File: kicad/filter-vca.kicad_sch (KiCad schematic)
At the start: 55 parts, among them J37 Conn_01x03_Male, U10 TL074, U12 LM13700, U13 LM13700, U15 TL072

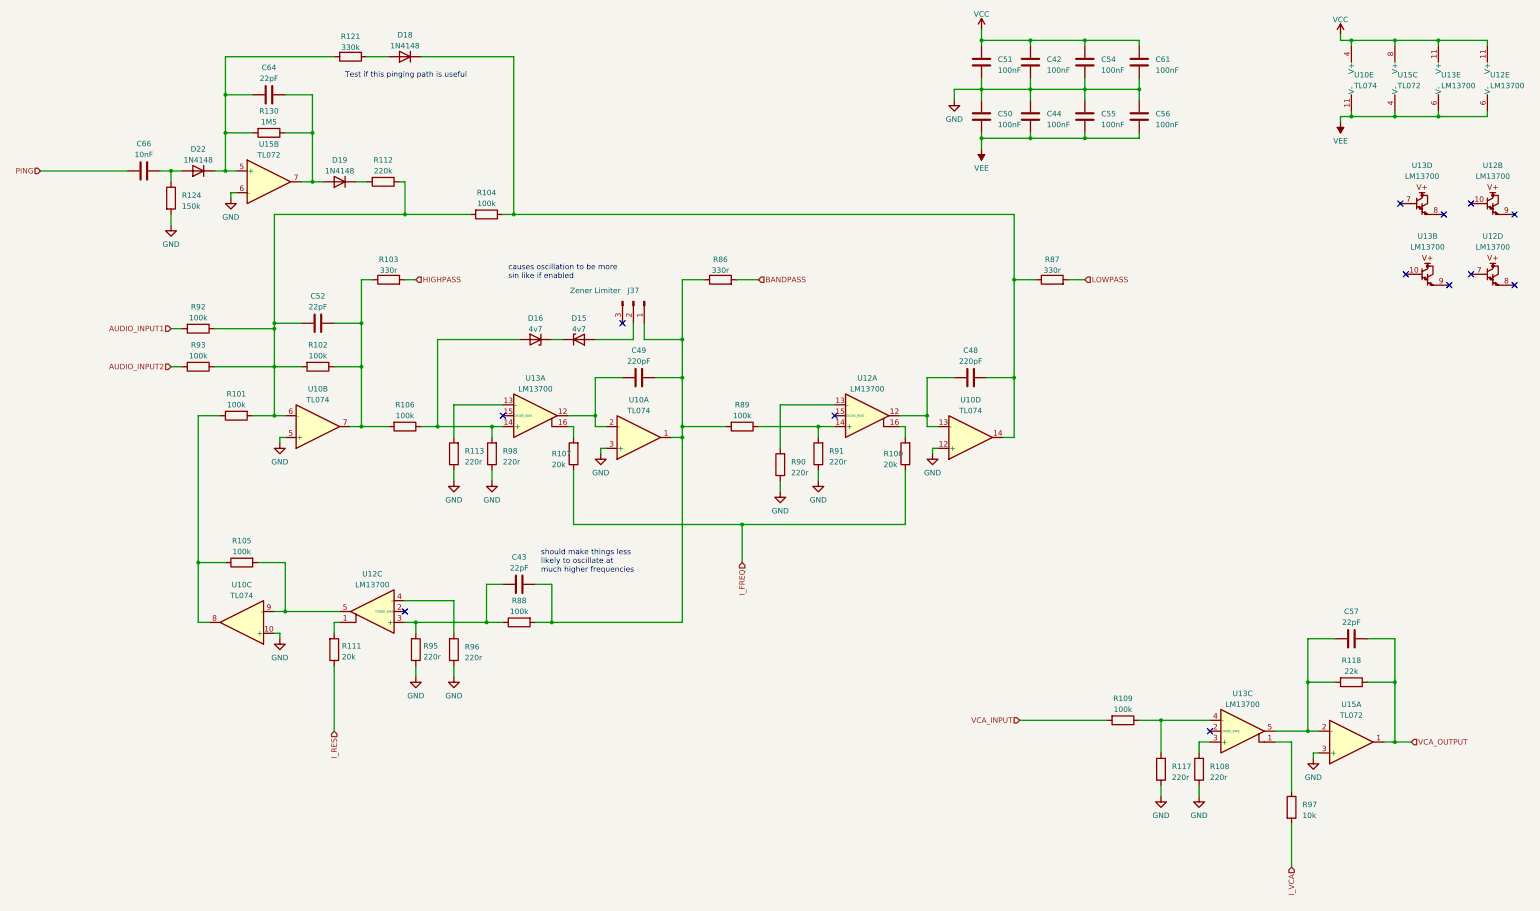
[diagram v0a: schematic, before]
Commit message: Minor tweaks to rev2 values
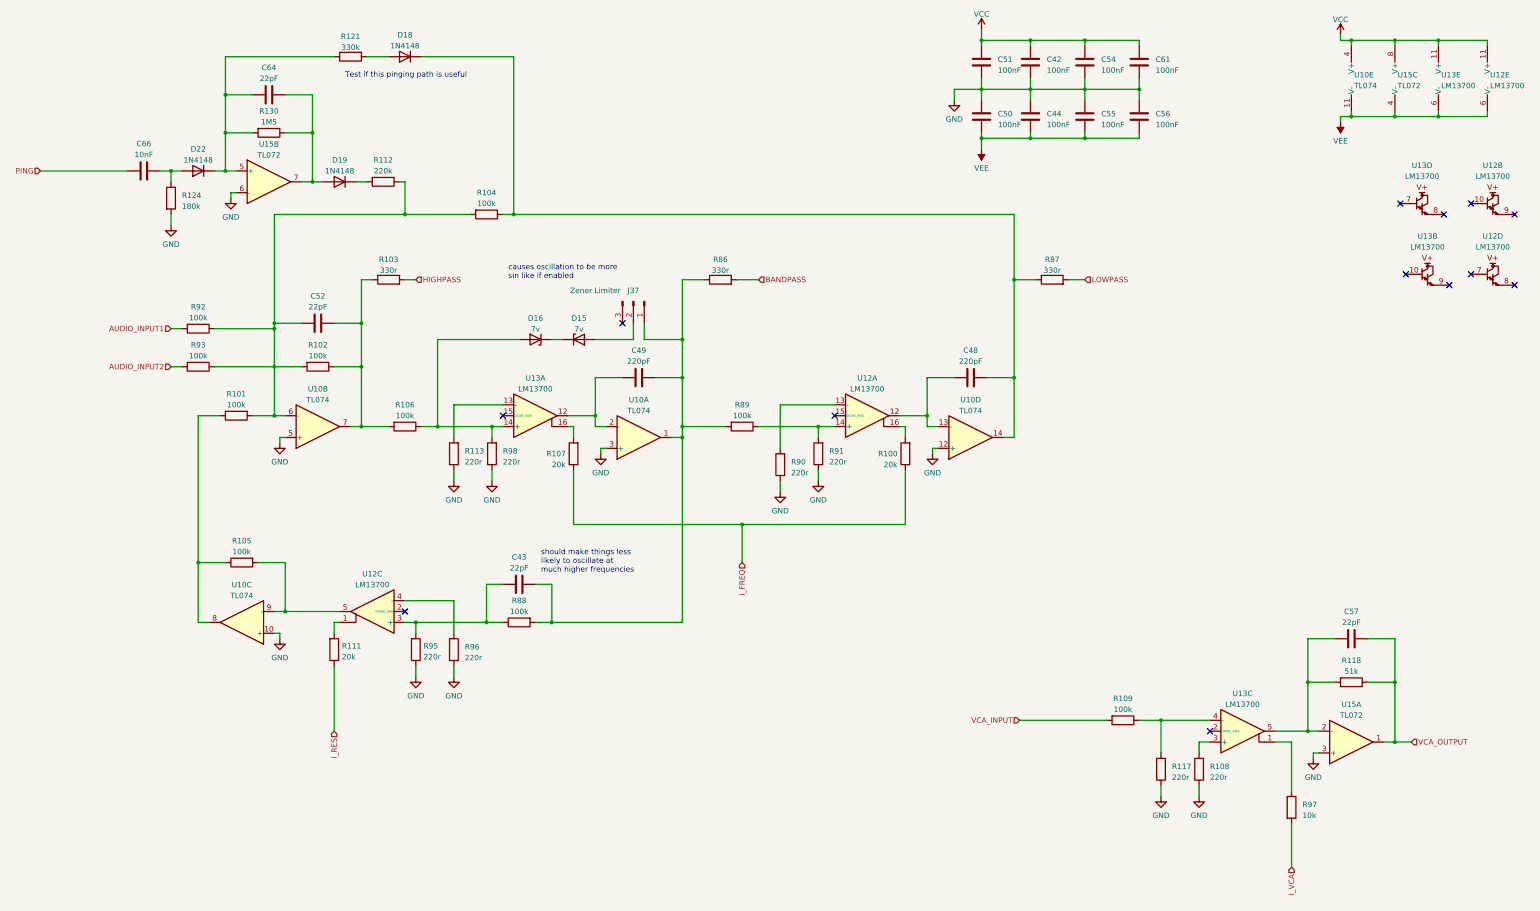
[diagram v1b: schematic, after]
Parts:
- D15, D16: value 4v7 -> 7v
- R118: value 22k -> 51k
- R124: value 150k -> 180k
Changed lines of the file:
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@@
   (symbol (lib_id "Rumblesan Standard Parts:R") (at 177.8 121.92 0) (unit 1)
     (in_bom yes) (on_board yes) (dnp no)
-    (property "Reference" "R107" (at 172.72 121.92 0)
+    (property "Reference" "R107" (at 171.45 121.92 0)
       (effects (font (size 1.27 1.27)) (justify left))
     )
@@
       (effects (font (size 1.27 1.27)))
     )
-    (property "Value" "4v7" (at 179.07 92.8171 0)
+    (property "Value" "7v" (at 179.07 92.8171 0)
       (effects (font (size 1.27 1.27)))
     )
@@
       (effects (font (size 1.27 1.27)))
     )
-    (property "Value" "4v7" (at 168.91 92.8171 0)
+    (property "Value" "7v" (at 168.91 92.8171 0)
       (effects (font (size 1.27 1.27)))
     )
@@
       (effects (font (size 1.27 1.27)))
     )
-    (property "Value" "22k" (at 359.41 172.72 90)
+    (property "Value" "51k" (at 359.41 172.72 90)
       (effects (font (size 1.27 1.27)))
     )
@@
       (effects (font (size 1.27 1.27)) (justify right))
     )
-    (property "Value" "150k" (at 86.36 64.135 0)
+    (property "Value" "180k" (at 86.36 64.135 0)
       (effects (font (size 1.27 1.27)) (justify right))
     )
@@
   (symbol (lib_id "Rumblesan Standard Parts:R") (at 255.27 121.92 0) (unit 1)
     (in_bom yes) (on_board yes) (dnp no)
-    (property "Reference" "R100" (at 250.19 121.92 0)
-      (effects (font (size 1.27 1.27)) (justify left))
-    )
+    (property "Reference" "R100" (at 248.92 121.92 0)
+      (effects (font (size 1.27 1.27)) (justify left))
+    )

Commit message: Updating zener values
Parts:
- D15, D16: value 7v -> 6v8; Spec 4.7v zener -> 6.8v zener
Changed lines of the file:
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@@
       (effects (font (size 1.27 1.27)))
     )
-    (property "Value" "7v" (at 179.07 92.8171 0)
+    (property "Value" "6v8" (at 179.07 92.8171 0)
       (effects (font (size 1.27 1.27)))
     )
@@
       (effects (font (size 1.27 1.27)) hide)
     )
-    (property "Spec" "4.7v zener" (at 179.07 95.25 0)
+    (property "Spec" "6.8v zener" (at 179.07 95.25 0)
+      (effects (font (size 1.27 1.27)) hide)
+    )
+    (property "Field5" "" (at 179.07 95.25 0)
       (effects (font (size 1.27 1.27)) hide)
     )
@@
       (effects (font (size 1.27 1.27)))
     )
-    (property "Value" "7v" (at 168.91 92.8171 0)
+    (property "Value" "6v8" (at 168.91 92.8171 0)
       (effects (font (size 1.27 1.27)))
     )
@@
       (effects (font (size 1.27 1.27)) hide)
     )
-    (property "Spec" "4.7v zener" (at 168.91 95.25 0)
+    (property "Spec" "6.8v zener" (at 168.91 95.25 0)
       (effects (font (size 1.27 1.27)) hide)
     )
+    (property "Field5" "" (at 168.91 95.25 0)
+      (effects (font (size 1.27 1.27)) hide)
+    )

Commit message: Changes after investigations and tweaking
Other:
- note removed: "Test if this pinging path is useful"
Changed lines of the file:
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@@
-    (effects (font (size 1.27 1.27)) (justify left bottom))
-  )
-  (text "Test if this pinging path is useful" (at 124.46 34.29 0)
     (effects (font (size 1.27 1.27)) (justify left bottom))
   )
